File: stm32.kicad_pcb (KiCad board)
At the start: 2 copper layers, 25 parts, among them CON1 BARREL_JACK, P1 CONN_01X11, P2 CONN_01X13, P3 CONN_01X08, P4 CONN_01X14, U1 STM32F103RB, U2 LD1117S33TR

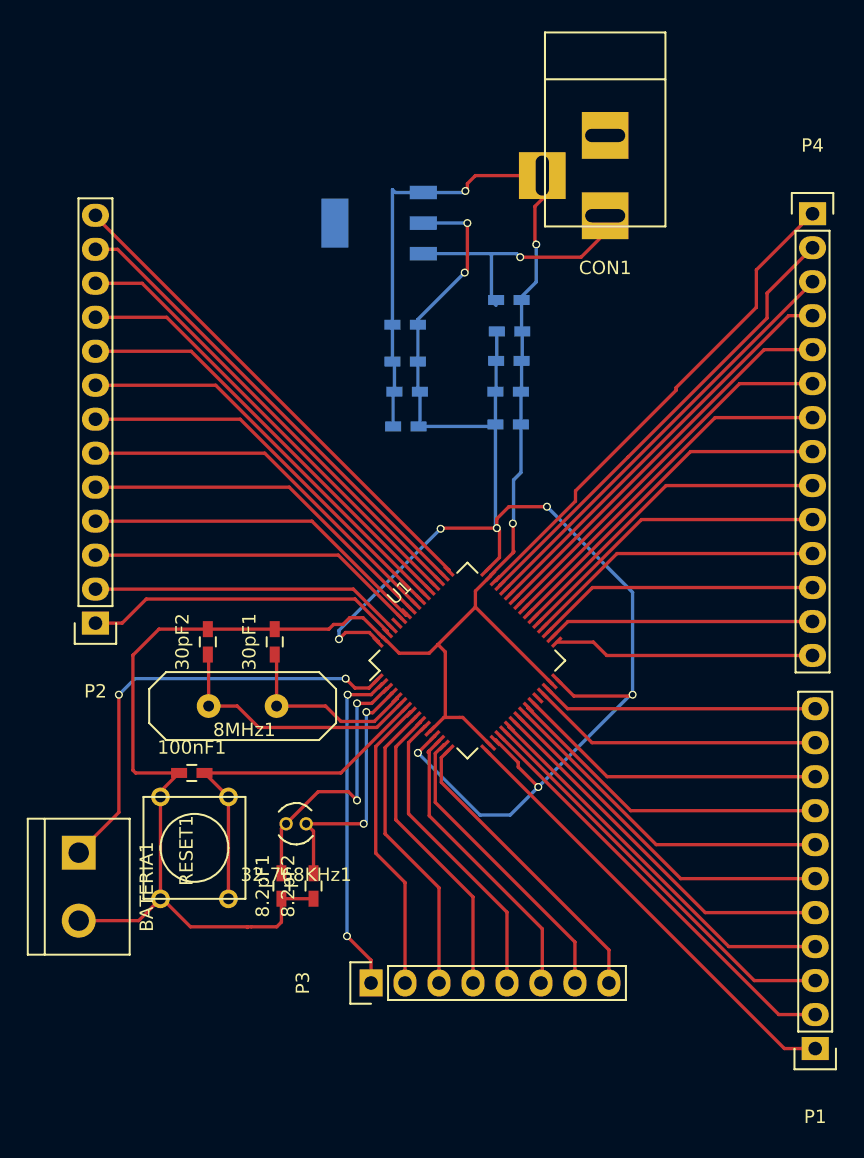
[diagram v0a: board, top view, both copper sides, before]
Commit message: ajustes
corrigido a inversão do valor com referencia
diminuido a largura da trilha.
trocado componentes por smd
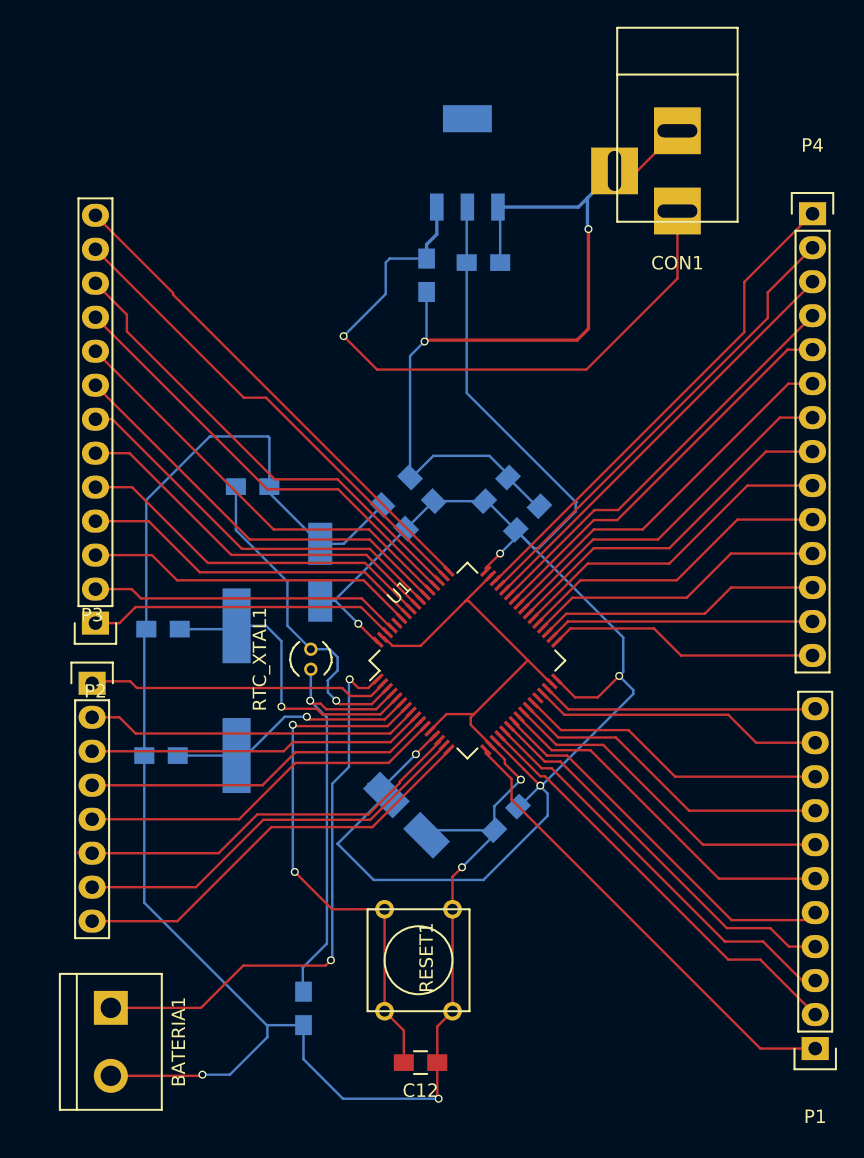
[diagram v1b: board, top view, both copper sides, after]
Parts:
- removed 100nF1, 100nF2, 100nF3, 100nF4, 100nF5, 10nF1, 30pF1, 30pF2, 8.2pF1, 8.2pF2: C, Capacitors_SMD:C_0603_HandSoldering
- removed 10uF1, 1uF1: CP, Capacitors_SMD:C_0603_HandSoldering
- removed 32.768KHz1: Crystal, Crystals:Crystal_Round_Vertical_3mm
- removed 8MHz1: Crystal, Crystals:HC-18UV
- added C10: 8.2pF, Capacitors_SMD:C_0805_HandSoldering, B.Cu at (139.3, 105.4)
- added C11: 8.2pF, Capacitors_SMD:C_0805_HandSoldering, B.Cu at (135.6, 66.4)
- added C12: 0.1uF, Capacitors_SMD:C_0805_HandSoldering, F.Cu at (148.1, 109.5)
- added C3: 0.1uF, Capacitors_SMD:C_0805_HandSoldering, B.Cu at (148.2, 66.6)
- added C4: 0.1uF, Capacitors_SMD:C_0805_HandSoldering, B.Cu at (154.5, 91.2)
- added C5: 0.1uF, Capacitors_SMD:C_0805_HandSoldering, B.Cu at (146.2, 68.7)
- added C6: 30pF, Capacitors_SMD:C_0805_HandSoldering, B.Cu at (128.7, 86.5)
- added C7: 30pF, Capacitors_SMD:C_0805_HandSoldering, B.Cu at (128.8, 77.0)
- added C8: 10u, Capacitors_SMD:C_0805_HandSoldering, B.Cu at (148.6, 50.6)
- added C9: 10u, Capacitors_SMD:C_0805_HandSoldering, B.Cu at (152.8, 49.6)
- added CP1: 10uF, Capacitors_Tantalum_SMD:TantalC_SizeB_EIA-3528_HandSoldering, B.Cu at (147.1, 91.0)
- added CP2: 1uF, Capacitors_Tantalum_SMD:TantalC_SizeB_EIA-3528_HandSoldering, B.Cu at (140.6, 72.8)
- added Main_Xtal1: 8MHz, Crystals:Crystal_HC49-SD_SMD, B.Cu at (134.3, 81.7)
- added RTC_XTAL1: 32.768KHz, Crystals:Crystal_Round_Vertical_3mm, F.Cu at (139.9, 79.3)
- C1: value 10u -> 10nF; footprint Capacitors_SMD:C_0603_HandSoldering -> Capacitors_SMD:C_0805_HandSoldering
- C2: value 10u -> 0.1uF; footprint Capacitors_SMD:C_0603_HandSoldering -> Capacitors_SMD:C_0805_HandSoldering
- moved P3 30.6 mm to (123.5, 81.1), turned to 0 degrees
- moved RESET1 18.7 mm to (147.9, 101.8), turned to 270 degrees
- moved C1 14.2 mm to (153.8, 66.6), turned to 45 degrees
- moved C2 14.0 mm to (156.1, 68.8), turned to 45 degrees
- moved BATERIA1 11.8 mm to (125.0, 107.9)
- moved U2 7.99 mm to (151.6, 42.2), turned to 180 degrees
- moved CON1 5.41 mm to (167.3, 39.6)
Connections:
- C1 pad 1: VCC -> +3V3
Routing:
- net GND: track 157.3 -> 236.7 mm, vias 3 -> 6
- net VCC: track 19.8 -> 48.0 mm
- net Net-(C10-Pad2): track 19.3 -> 32.4 mm, vias 2 -> 1
- net +3V3: track 119.7 -> 132.7 mm, vias 9 -> 5
- net Net-(C12-Pad2): track 27.3 -> 40.1 mm, vias 0 -> 2
- net /PA2: track 22.8 -> 32.0 mm
- net /VBAT: track 33.5 -> 42.2 mm
- net /PA1: track 22.4 -> 30.7 mm
- net Net-(C7-Pad1): track 14.2 -> 22.5 mm, vias 0 -> 1
- net /PA0: track 22.1 -> 29.6 mm
- net /PC3: track 22.8 -> 27.8 mm
- net Net-(C11-Pad1): track 20.8 -> 25.0 mm, vias 2 -> 1
- net /PC2: track 22.7 -> 26.6 mm
- net /PC1: track 22.5 -> 25.3 mm
- net /PC0: track 22.3 -> 25.0 mm
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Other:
- net class fina added: clearance 0.2, trace_width 0.18, via_dia 0.6, via_drill 0.4
- rule trace_min: 0.2 -> 0.18
